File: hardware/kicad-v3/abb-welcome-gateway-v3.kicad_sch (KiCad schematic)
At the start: 72 parts, among them P1 WJ500V-5.08-2P, Q1 S8050, Q2 S8050, Q3 S8050, Q4 2N7002, Q5 2N7002, Q6 2N7002, SW1 TS-1187A-B-A-B, U1 TPS5430DDAR, U2 ESP32-S3-WROOM-1-N16R8, U3 74LVC1G14

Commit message: KiCad 9: re-guardado del proyecto v3 en formato nativo (baseline pre-ruteo)
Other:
- moved on the sheet: R20, R8

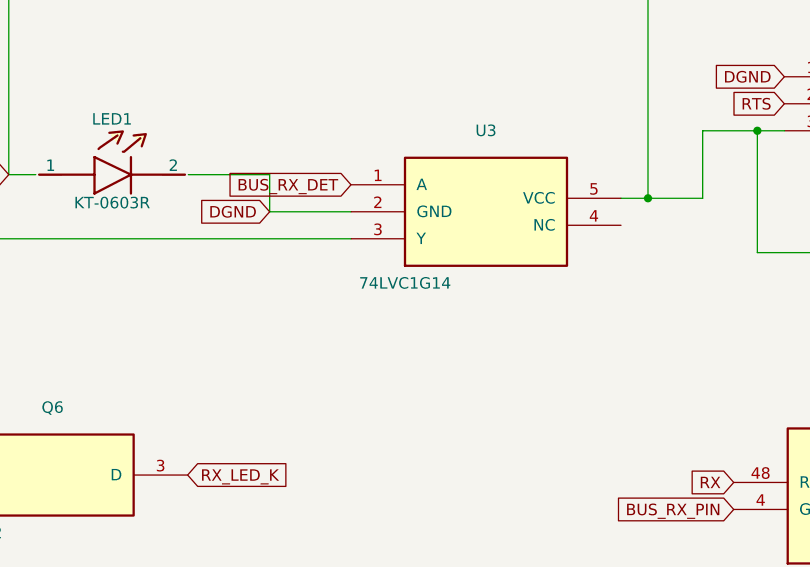
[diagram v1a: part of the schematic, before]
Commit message: fab: specify exact parts for P2 (1x6 2.54mm header) and U3 (SN74LVC1G14DBVR)
Both carried generic placeholders from the tscircuit conversion. Set the
manufacturer part in the symbol Value + footprint identity in schematic and
PCB, and refresh the BOM/pos exports. Metadata only; no copper change, DRC
still 0 errors / 0 unconnected. Documented in docs/STATUS.md.
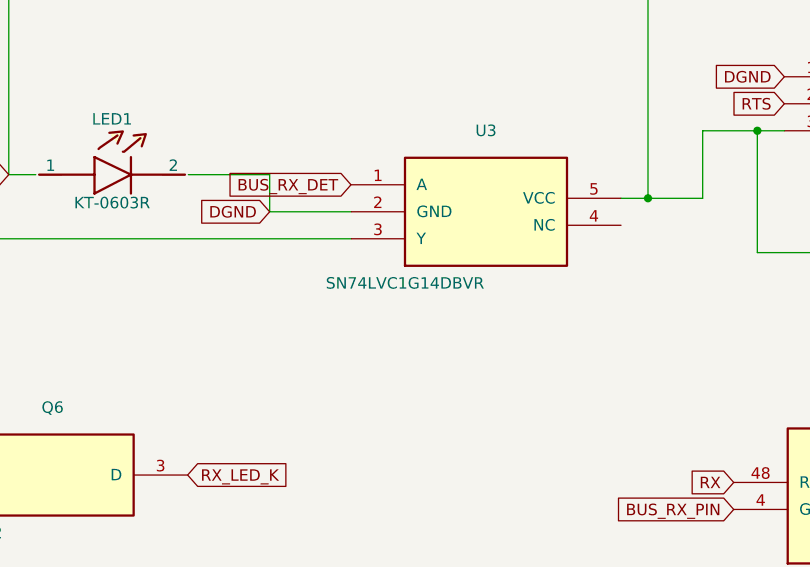
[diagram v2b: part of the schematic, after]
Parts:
- P2: value (none) -> 61300611121; footprint (none) -> tscircuit:PinHeader_1x06_2.54mm
- U3: value 74LVC1G14 -> SN74LVC1G14DBVR; footprint (none) -> tscircuit:SOT-23-5
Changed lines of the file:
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@@
 			)
 		)
-		(property "Value" "74LVC1G14"
+		(property "Value" "SN74LVC1G14DBVR"
 			(at 386.675 285.0538 0)
 			(effects
@@
 			)
 		)
-		(property "Footprint" ""
+		(property "Footprint" "tscircuit:SOT-23-5"
 			(at 393.897 277.1038 90)
 			(effects
@@
 			)
 		)
-		(property "Value" ""
+		(property "Value" "61300611121"
 			(at 437.825 271.1038 0)
 			(effects
@@
 			)
 		)
-		(property "Footprint" ""
+		(property "Footprint" "tscircuit:PinHeader_1x06_2.54mm"
 			(at 436.047 265.1038 90)
 			(effects
